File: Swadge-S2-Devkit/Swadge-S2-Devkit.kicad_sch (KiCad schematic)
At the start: 100 parts, among them J1 SAO, J2 DEBUG, J3 Conn_01x05_Male, P1 USB_C_Plug_USB2.0, Q1 Q_PMOS_GSD, SW1 TS-1109S-A-A, SW2 TS-1109S-A-A, SW3 TS-1109S-A-A, SW4 TS-1109S-A-A, SW5 TS-1109S-A-A, SW6 TS-1109S-A-A, SW7 B3FS-4002P, SW8 B3FS-4002P, SW9 SW_SPDT_1825232-1, U1 ESP32-S2-SOLO, U2 RB017A1505A, U3 MT3410, U4 RB0154A1201A, U5 RB017A1505A_Connector, U6 Controller_Shields, U7 GENERIC_LDO_2.8, U8 QMA7981

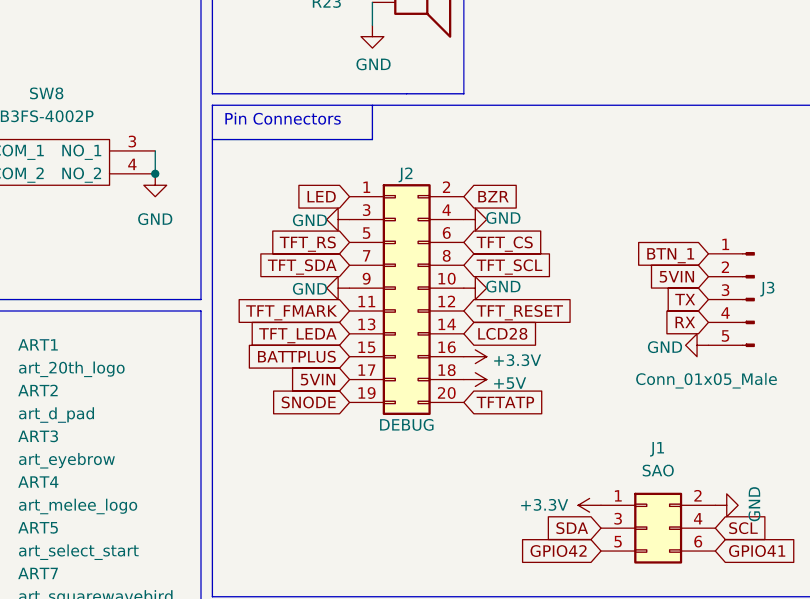
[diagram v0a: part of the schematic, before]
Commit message: Removed 20 pin monstrosity, rerouted
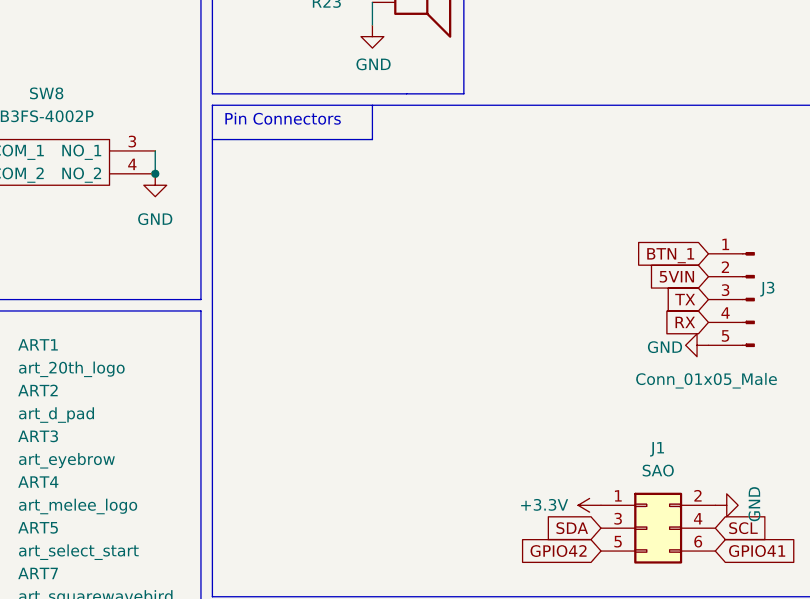
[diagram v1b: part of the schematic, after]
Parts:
- removed J2: DEBUG, Swadge_Parts:PinHeader_2x10_P2.54mm_Vertical, symbol Swadge_Parts:Conn_02x10_Odd_Even

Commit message: Bump swadge.
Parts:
- removed C28: 2.2μF, Swadge_Parts:C_0603_1608Metric, symbol Swadge_Parts:C
- added C28, C30: (no value), symbol Device:C
- added C29, C31, C32, C33, C34, C35: 100nSpc, Capacitor_SMD:C_1210_3225Metric_Pad1.33x2.70mm_HandSolder, symbol Device:C
- D5, D6, D7, D8: value SK6812-SIDE-D -> (none); footprint Swadge_Parts:SK6812D_SIDE -> (none); LCSC C2890037 -> C2890041
- J1: value SAO -> (none); footprint Swadge_Parts:PinHeader_2x03_P2.54mm_Vertical -> (none)
- J3: value Conn_01x05_Male -> PGM
- R12, R18: value 47Ω -> 0Ω; LCSC C254549 -> C21189
- U1: value ESP32-S2-SOLO -> (none); footprint Swadge_Parts:ESP32-S2-SOLO -> (none); LCSC (none) -> C3013947
- U5: value RB017A1505A_Connector -> (none); footprint Swadge_Parts:HCTL HC-FPC-03-10-15RLTAG -> (none); LCSC C3012328 -> C3029632
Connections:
- net GPIO3 is gone; now on net SDA: U1.15 (GPIO3/TOUCH3/ADC1_CH2)
- net +3V3: now also R10.2, R11.1, U6.11, U6.2, U6.4, U6.6, U6.7, U6.9, C28.1, C29.1, C30.1, C31.1, C32.1, C33.1, C34.1, C35.1; no longer R10.1, R11.2
- net GND: now also U6.1, U6.10, U6.12, U6.3, U6.5, U6.8, C28.2, C29.2, C30.2, C31.2, C32.2, C33.2, C34.2, C35.2
- net SCL: now also R11.2, U1.34 (MTDI/GPIO41/CLK_OUT1); no longer R11.1, U1.11 (GPIO18/U1RXD/ADC2_CH7/DAC_2/CLK_OUT3)
- net SDA: now also R10.1; no longer R10.2, U1.10 (GPIO17/U1TXD/ADC2_CH6/DAC_1)
- net GPIO41 renamed GPIO18
- net GPIO18: now also U1.11 (GPIO18/U1RXD/ADC2_CH7/DAC_2/CLK_OUT3); no longer U1.34 (MTDI/GPIO41/CLK_OUT1)
- net GPIO42: no longer names the net of U1.35 (MTMS/GPIO42)
- net GPIO42: no longer J1.5 (Pin_5)
- new net GPIO17: J1.5 (Pin_5), U1.10 (GPIO17/U1TXD/ADC2_CH6/DAC_1)
- no-connect marks 24 -> 13
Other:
- note removed: "TODO Use other footprint for LEDs"
- moved on the sheet: J1

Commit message: Moved battery lower. Placed SAO
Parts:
- removed U4: RB0154A1201A, Swadge_Parts:LCD_240x240_1.54_12, symbol Swadge_Parts:RB0154A1201A
- C28, C30: value (none) -> 100nSpc; footprint (none) -> Capacitor_SMD:C_1210_3225Metric_Pad1.33x2.70mm_HandSolder
- D5, D6, D7, D8: value (none) -> SK6812-SIDE-D; footprint (none) -> Swadge_Parts:SK6812D_SIDE
- J1: value (none) -> SAO; footprint (none) -> Swadge_Parts:PinSocket_2x03_P2.54mm_Vertical
- U1: value (none) -> ESP32-S2-SOLO; footprint (none) -> Swadge_Parts:ESP32-S2-SOLO
- U5: value (none) -> RB017A1505A_Connector; footprint (none) -> Swadge_Parts:HCTL HC-FPC-03-10-15RLTAG

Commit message: * Add Slider (remove center touch)  * Route board
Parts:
- removed R16: 680Ω, Swadge_Parts:R_0603_1608Metric, symbol Swadge_Parts:R_US
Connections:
- no-connect marks 13 -> 14
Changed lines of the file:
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@@
   (no_connect (at 25.4 172.72))
   (no_connect (at 156.845 187.96))
+  (no_connect (at 175.26 148.59))
   (no_connect (at 44.45 67.31))
   (no_connect (at 44.45 69.85))
@@
     (pin "4")
   )
-  (symbol (lib_id "Swadge_Parts:R_US") (at 179.07 148.59 270) (unit 1)
-    (in_bom yes) (on_board yes)
-    (property "Reference" "R16" (id 0) (at 185.42 147.32 90)
-      (effects (font (size 1.27 1.27)) (justify right))
-    )
-    (property "Value" "680Ω" (id 1) (at 180.34 143.51 90)
-      (effects (font (size 1.27 1.27)) (justify right) hide)
-    )
-    (property "Footprint" "Swadge_Parts:R_0603_1608Metric" (id 2) (at 178.816 149.606 90)
-      (effects (font (size 1.27 1.27)) hide)
-    )
-    (property "Datasheet" "~" (id 3) (at 179.07 151.13 90)
-      (effects (font (size 1.27 1.27)) hide)
-    )
-    (property "Digikey" "~" (id 4) (at 181.61 153.67 90)
-      (effects (font (size 1.27 1.27)) hide)
-    )
-    (property "Cost100" "10" (id 5) (at 179.07 148.59 0)
-      (effects (font (size 0.254 0.254)) hide)
-    )
-    (property "Substitutable" "Y" (id 6) (at 179.07 148.59 0)
-      (effects (font (size 0.254 0.254)) hide)
-    )
-    (property "LCSC" "C23228" (id 7) (at 179.07 148.59 0)
-      (effects (font (size 1.27 1.27)) hide)
-    )
-    (pin "1")
-    (pin "2")
-  )
   (symbol (lib_id "Swadge_Parts:RB017A1505A") (at 334.01 92.71 0) (unit 1)
     (in_bom yes) (on_board yes)
@@
       (reference "R15") (unit 1) (value "680Ω") (footprint "Swadge_Parts:R_0603_1608Metric")
     )
-    (path "/b74bc0a1-0ab1-4fa8-a5a5-f45b5a2846d3"
-      (reference "R16") (unit 1) (value "680Ω") (footprint "Swadge_Parts:R_0603_1608Metric")
-    )
     (path "/465762c7-7ff2-4bd9-b39e-b3a551d1ae0a"

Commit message: Forgot to update schematic to reflect change with touch sensor.
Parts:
- ART6: value art_xy_buttons -> (none); footprint Swadge_Parts:XY_Buttons -> (none)
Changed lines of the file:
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@@
       (effects (font (size 1.27 1.27)) (justify left))
     )
-    (property "Value" "art_xy_buttons" (id 1) (at 193.04 148.59 0)
+    (property "Value" "" (id 1) (at 193.04 148.59 0)
       (effects (font (size 1.27 1.27)) (justify left))
     )
-    (property "Footprint" "Swadge_Parts:XY_Buttons" (id 2) (at 187.96 137.16 0)
+    (property "Footprint" "" (id 2) (at 187.96 137.16 0)
       (effects (font (size 1.27 1.27)) hide)
     )
@@
     )
     (path "/124ba641-cee9-4e92-be15-b26f5356268e"
-      (reference "ART6") (unit 1) (value "art_xy_buttons") (footprint "Swadge_Parts:XY_Buttons")
+      (reference "ART6") (unit 1) (value "art_xy_buttons") (footprint "Swadge_Parts:XY_Buttons2")
     )
     (path "/50423250-2217-49e3-9e3d-d8972fba598e"

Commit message: Use C 1210 from Swadge-Parts
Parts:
- ART6: value (none) -> art_xy_buttons; footprint (none) -> Swadge_Parts:XY_Buttons2
- C28, C29, C30, C31, C32, C33, C34, C35: footprint Capacitor_SMD:C_1210_3225Metric_Pad1.33x2.70mm_HandSolder -> Swadge_Parts:C_1210_3225Metric_Pad1.33x2.70mm_HandSolder; symbol Device:C -> Swadge_Parts:C; Cost100 (none) -> 10; Substitutable (none) -> Y

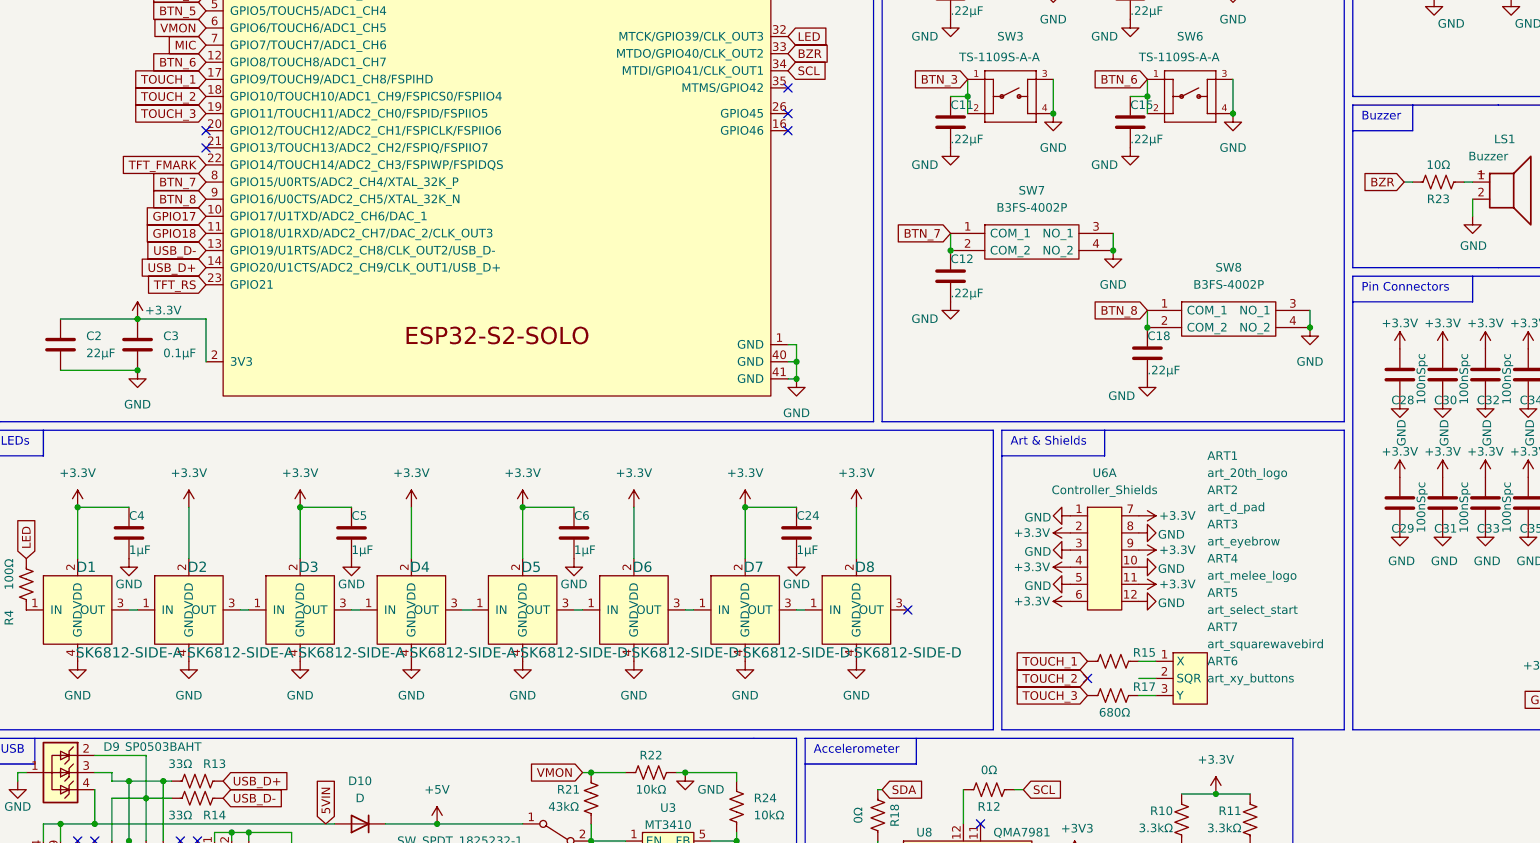
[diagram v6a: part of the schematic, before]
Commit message: Place and route touch bar
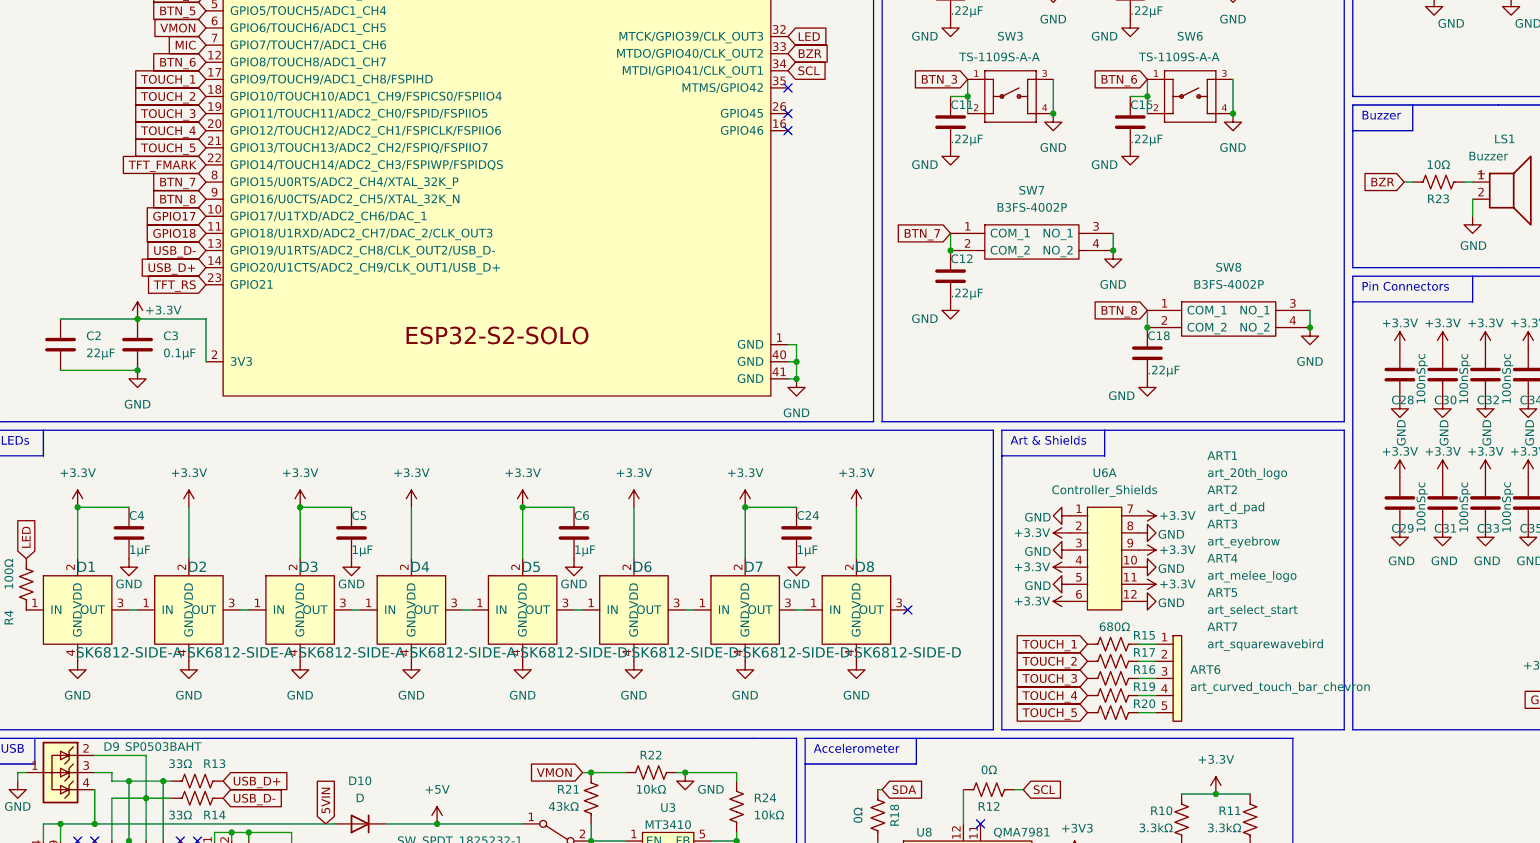
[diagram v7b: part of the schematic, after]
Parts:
- removed ART6: art_xy_buttons, Swadge_Parts:XY_Buttons2, symbol Swadge_Parts:art_xy_buttons
- added ART6: art_curved_touch_bar_chevron, Swadge_Parts:curved-touch-bar-chevrons, symbol Swadge_Parts:art_curved_touch_bar_chevron
- added R16, R19, R20: 680Ω, Swadge_Parts:R_0603_1608Metric, symbol Swadge_Parts:R_US
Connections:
- net TOUCH_2: now also R17.2
- net TOUCH_3: now also R16.2; no longer R17.2
- net at R15.1: now also ART6.1
- net at R17.1: now also ART6.2
- net TOUCH_4: now reaches U1.20 (GPIO12/TOUCH12/ADC2_CH1/FSPICLK/FSPIIO6)
- net TOUCH_4: now also R19.2
- net TOUCH_5: now reaches U1.21 (GPIO13/TOUCH13/ADC2_CH2/FSPIQ/FSPIIO7)
- net TOUCH_5: now also R20.2
- new net: ART6.3, R16.1
- new net: ART6.4, R19.1
- new net: ART6.5, R20.1
- no-connect marks 14 -> 11
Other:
- moved on the sheet: R15, R17

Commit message: fix LCSC part number
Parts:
- U5: LCSC C3029632 -> C3012328
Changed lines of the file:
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@@
       (effects (font (size 1.27 1.27)) hide)
     )
-    (property "LCSC" "C3029632" (id 8) (at 311.785 67.31 0)
+    (property "LCSC" "C3012328" (id 8) (at 311.785 67.31 0)
       (effects (font (size 1.27 1.27)) hide)
     )
